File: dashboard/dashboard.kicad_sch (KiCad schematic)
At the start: 76 parts, among them J1 FUNC1_BTN, J10 PROG, J11 RGB, J12 5V_IN, J13 CAN, J14 PWR, J2 FUNC2_BTN, J3 FUNC3_BTN, J4 FAULT1_LED, J5 FAULT2_LED, J6 FAULT3_LED, J7 FUNC1_LED, J8 FUNC2_LED, J9 FUNC3_LED, Q1 2N7002, Q2 2N7002, Q3 2N7002, Q4 2N7002, Q5 2N7002, Q6 2N7002, SW1 SW_SPST, U1 FODM217D, U2 FODM217D, U3 FODM217D, U4 STM32F103C8Tx, U5 AP2204K-ADJ, U6 SN65HVD256D, U7 AP2204K-ADJ, Y1 8M, Y2 32.768k

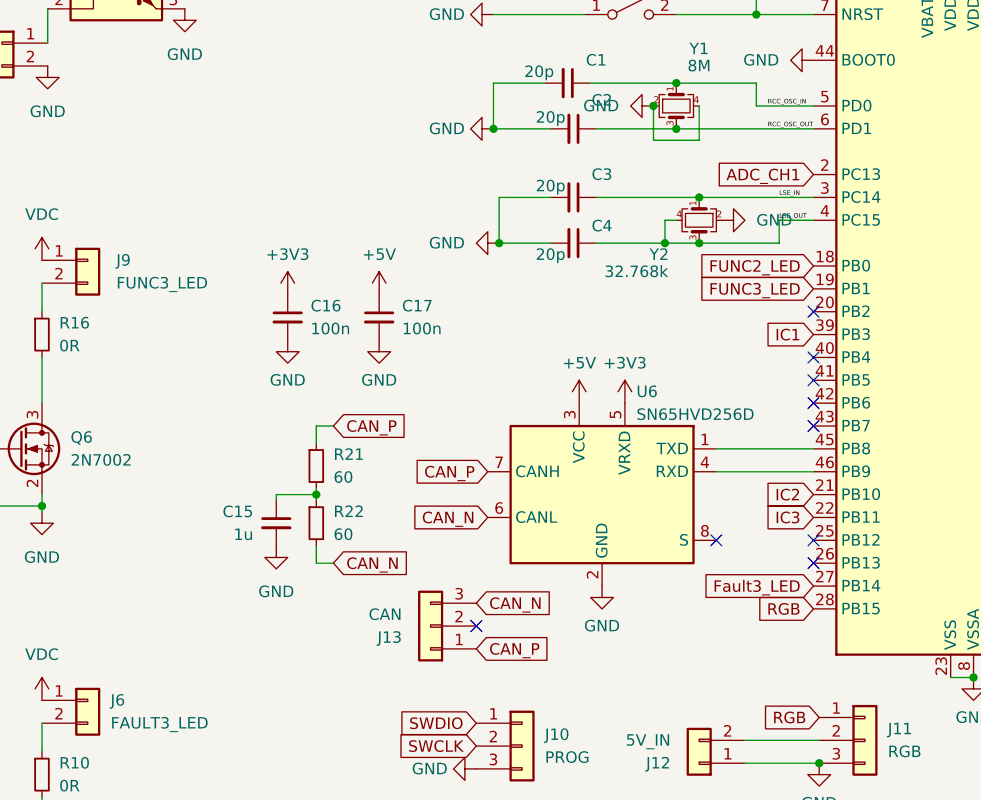
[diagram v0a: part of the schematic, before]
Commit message: fix: can jumper
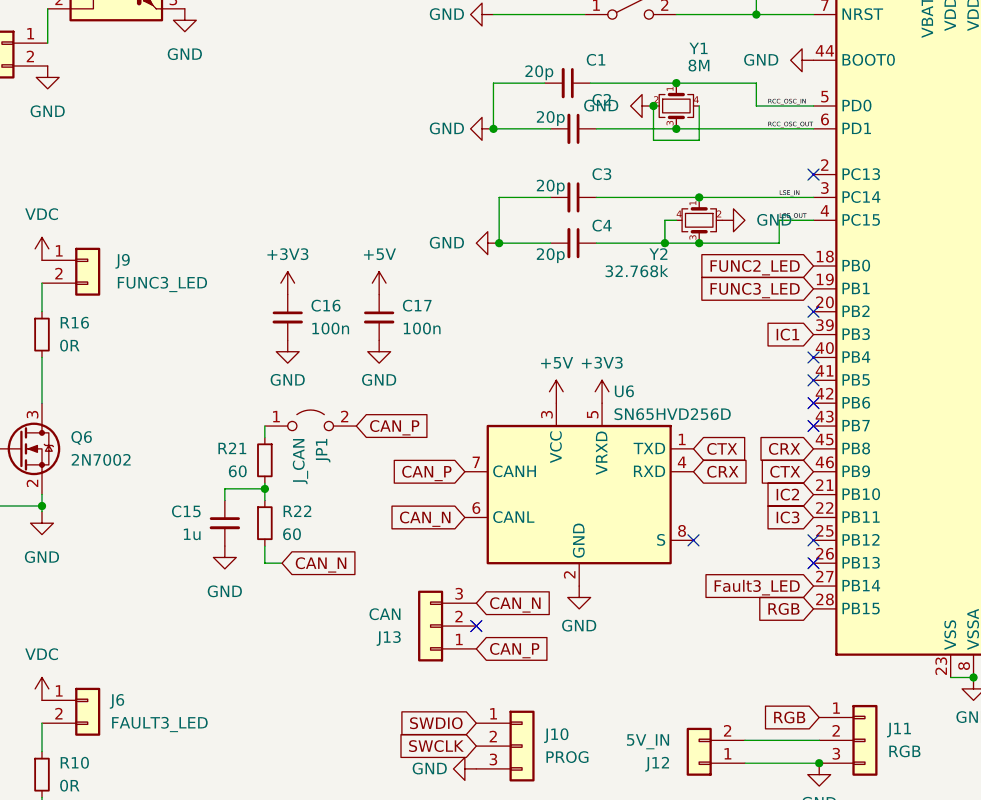
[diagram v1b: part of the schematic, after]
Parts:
- added JP1: J_CAN, PCM_Jumper_AKL:Jumper_P2.54mm_D0.7mm, symbol Jumper:Jumper_2_Open
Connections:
- net CAN_P: now also JP1.2 (B); no longer R21.1
- net CRX: now reaches U4.45 (PB8)
- net CRX: now also U6.4 (RXD); no longer U6.1 (TXD)
- net CTX: now reaches U4.46 (PB9)
- net CTX: now also U6.1 (TXD); no longer U6.4 (RXD)
- net ADC_CH1: no longer names the net of U4.2 (PC13)
- new net: JP1.1 (A), R21.1
- no-connect marks 10 -> 11
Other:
- moved on the sheet: C15, R21, R22, U6

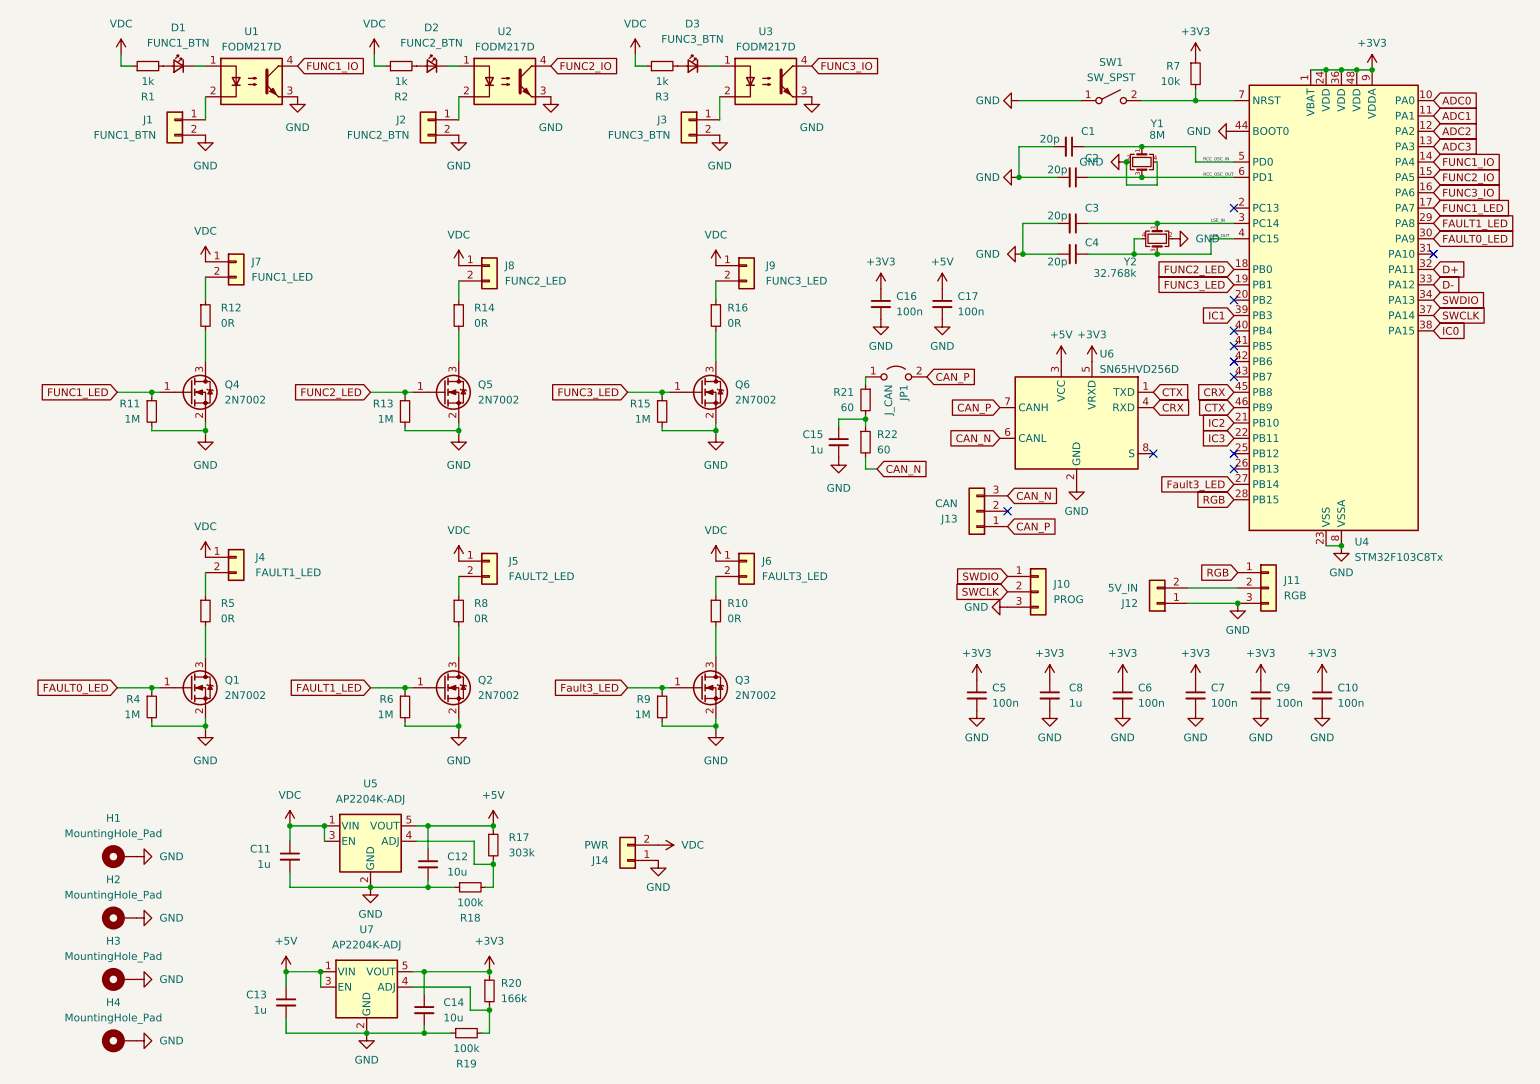
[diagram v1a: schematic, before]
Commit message: fix: dashboard CAN
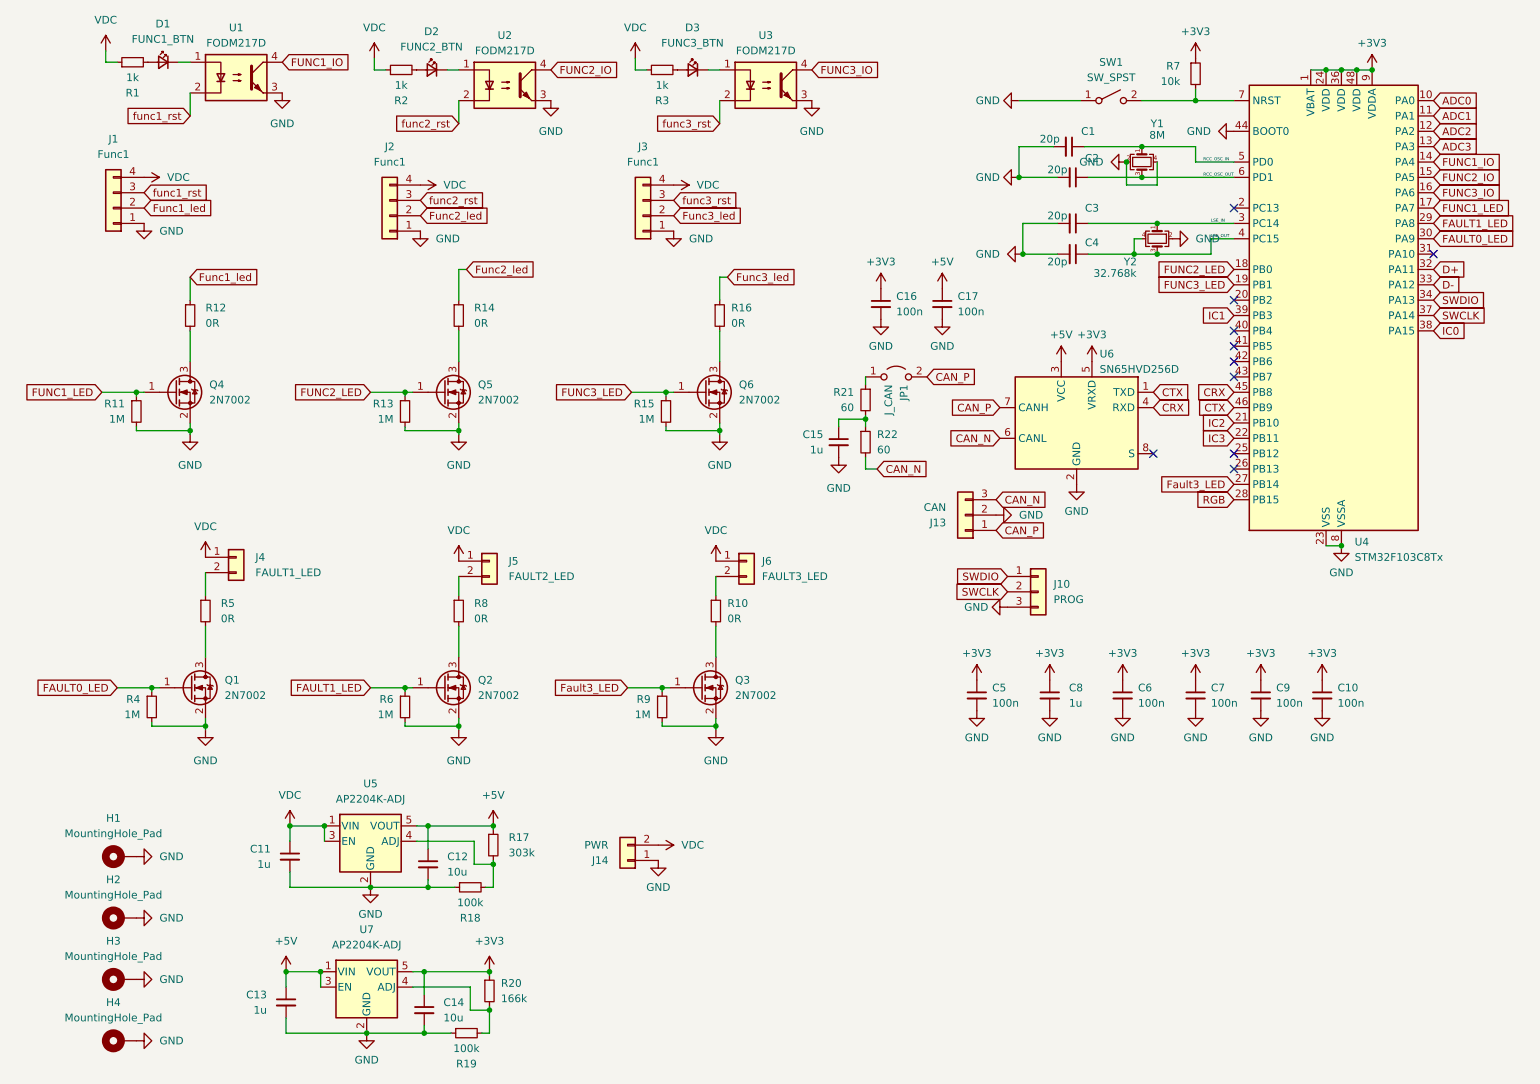
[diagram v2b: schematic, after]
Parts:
- removed J1: FUNC1_BTN, Connector_JST:JST_XH_B2B-XH-A_1x02_P2.50mm_Vertical, symbol Connector_Generic:Conn_01x02
- removed J11: RGB, Connector_JST:JST_XH_B3B-XH-A_1x03_P2.50mm_Vertical, symbol Connector_Generic:Conn_01x03
- removed J12: 5V_IN, Connector_JST:JST_XH_B2B-XH-A_1x02_P2.50mm_Vertical, symbol Connector_Generic:Conn_01x02
- removed J2: FUNC2_BTN, Connector_JST:JST_XH_B2B-XH-A_1x02_P2.50mm_Vertical, symbol Connector_Generic:Conn_01x02
- removed J3: FUNC3_BTN, Connector_JST:JST_XH_B2B-XH-A_1x02_P2.50mm_Vertical, symbol Connector_Generic:Conn_01x02
- removed J7: FUNC1_LED, Connector_JST:JST_XH_B2B-XH-A_1x02_P2.50mm_Vertical, symbol Connector_Generic:Conn_01x02
- removed J8: FUNC2_LED, Connector_JST:JST_XH_B2B-XH-A_1x02_P2.50mm_Vertical, symbol Connector_Generic:Conn_01x02
- removed J9: FUNC3_LED, Connector_JST:JST_XH_B2B-XH-A_1x02_P2.50mm_Vertical, symbol Connector_Generic:Conn_01x02
- added J1, J2, J3: Func1, Connector_JST:JST_XH_B4B-XH-A_1x04_P2.50mm_Vertical, symbol Connector_Generic:Conn_01x04
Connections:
- net GND: now also J13.2 (Pin_2), J1.1 (Pin_1), J2.1 (Pin_1), J3.1 (Pin_1)
- net VDC: now also J1.4 (Pin_4), J2.4 (Pin_4), J3.4 (Pin_4)
- net func1_rst: now reaches U1.2
- net func1_rst: now also J1.3 (Pin_3)
- net func2_rst: now reaches U2.2
- net func2_rst: now also J2.3 (Pin_3)
- net Func3_led: now reaches R16.1
- net Func3_led: now also J3.2 (Pin_2)
- net Func2_led: now reaches R14.1
- net Func2_led: now also J2.2 (Pin_2)
- net func3_rst: now reaches U3.2
- net func3_rst: now also J3.3 (Pin_3)
- net Func1_led: now reaches R12.1
- net Func1_led: now also J1.2 (Pin_2)
- no-connect marks 11 -> 10
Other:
- moved on the sheet: D1, D2, D3, J13, Q4, Q6, R1, R11, R12, R15, R16, R2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
